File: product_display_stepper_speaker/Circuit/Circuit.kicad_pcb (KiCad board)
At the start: 2 copper layers, 1 part, among them U1 Pico

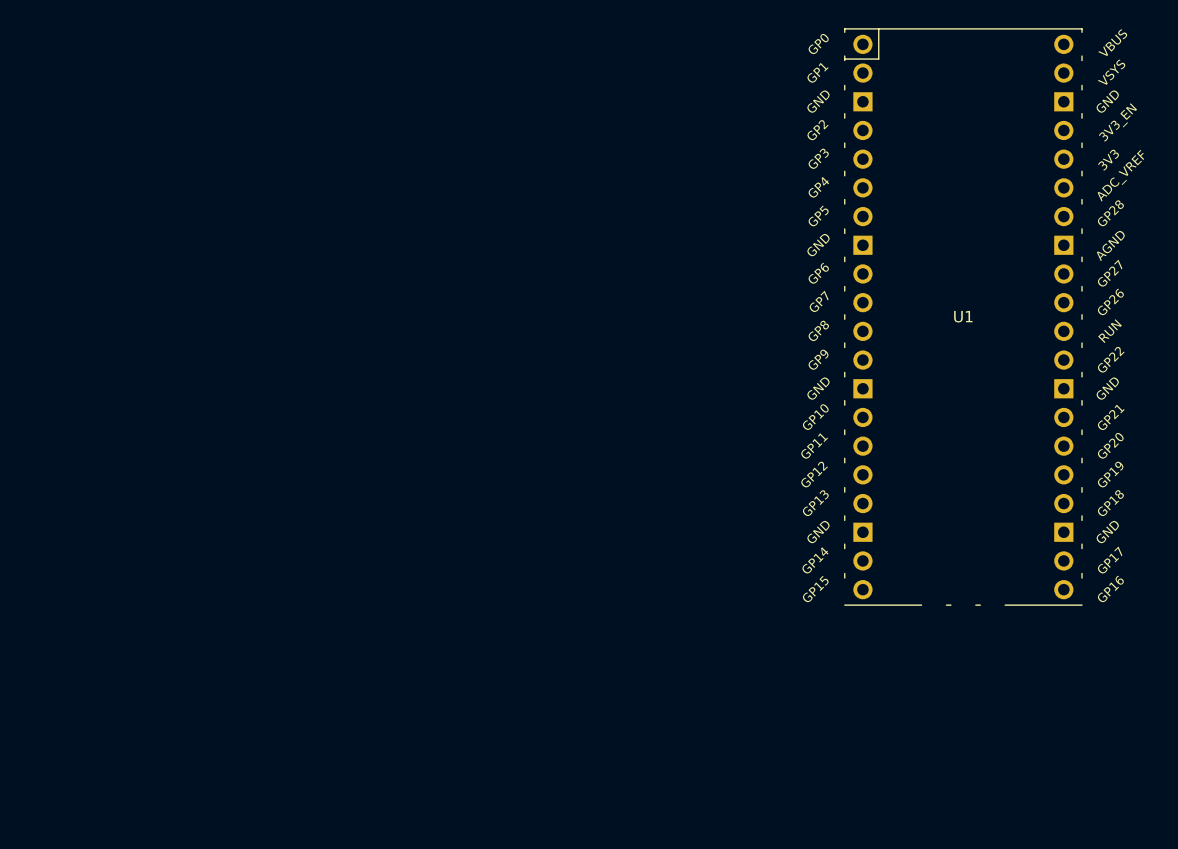
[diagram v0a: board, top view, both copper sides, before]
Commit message: finished circuit schematic and started pcb layout of product speaker stepper project
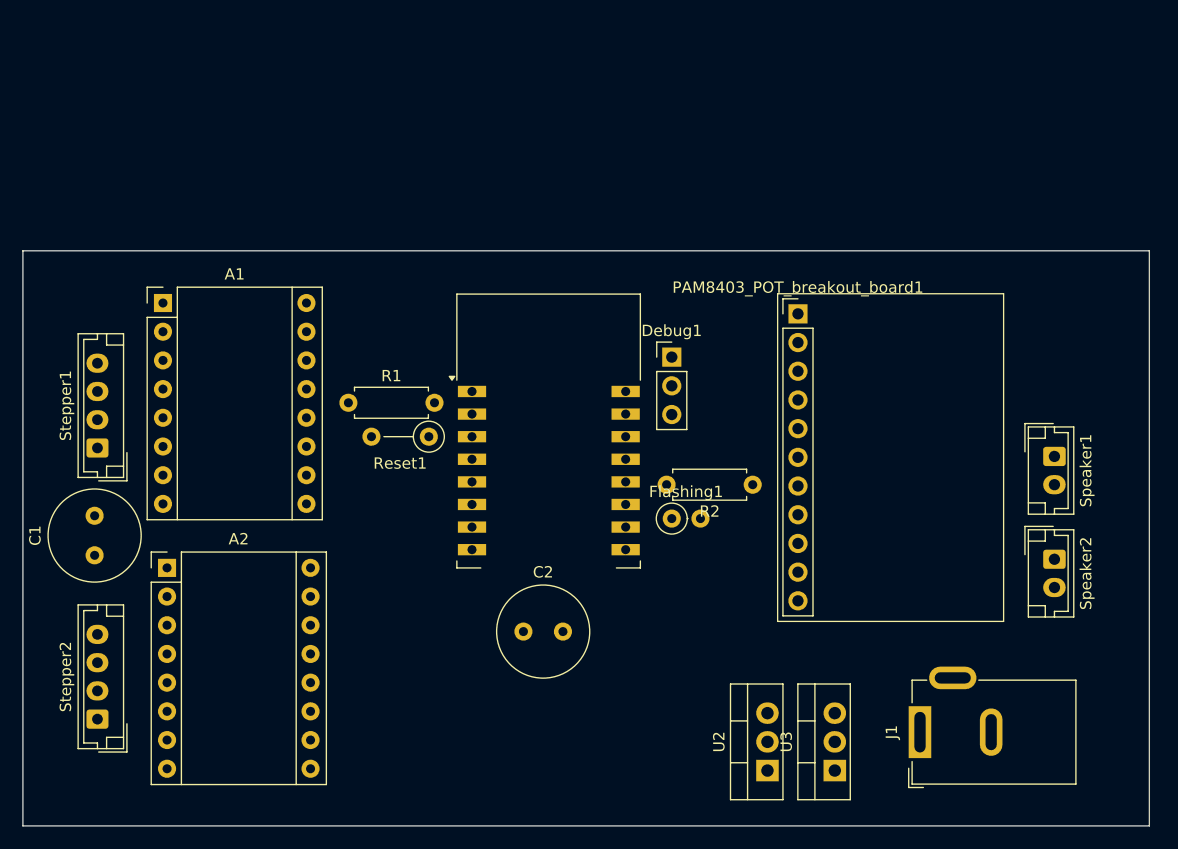
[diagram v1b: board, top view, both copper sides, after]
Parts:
- added A1: Pololu_Breakout_DRV8825, Module:Pololu_Breakout-16_15.2x20.3mm, F.Cu at (71.8, 94.4)
- added A2: Pololu_Breakout_DRV8825, Module:Pololu_Breakout-16_15.2x20.3mm, F.Cu at (72.2, 117.9)
- added C1: 470uf, Capacitor_THT:C_Radial_D8.0mm_H11.5mm_P3.50mm, F.Cu at (65.8, 116.8)
- added C2: 330uf, Capacitor_THT:C_Radial_D8.0mm_H11.5mm_P3.50mm, F.Cu at (103.7, 123.5)
- added Debug1: Conn_1x3, Connector_PinHeader_2.54mm:PinHeader_1x03_P2.54mm_Vertical, F.Cu at (116.8, 99.2)
- added Flashing1: Headers, Resistor_THT:R_Axial_DIN0207_L6.3mm_D2.5mm_P2.54mm_Vertical, F.Cu at (116.8, 113.5)
- added J1: Barrel_Jack_MountingPin, Connector_BarrelJack:BarrelJack_GCT_DCJ200-10-A_Horizontal, F.Cu at (138.8, 132.4)
- added PAM8403_POT_breakout_board1: Conn_01x11, Connector_PinHeader_2.54mm:PinHeader_1x11_P2.54mm_Vertical, F.Cu at (128.0, 95.4)
- added R1: 10k, Resistor_THT:R_Axial_DIN0207_L6.3mm_D2.5mm_P7.62mm_Horizontal, F.Cu at (88.2, 103.2)
- added R2: 10k, Resistor_THT:R_Axial_DIN0207_L6.3mm_D2.5mm_P7.62mm_Horizontal, F.Cu at (124.0, 110.5)
- added Reset1: Button, Resistor_THT:R_Axial_DIN0207_L6.3mm_D2.5mm_P5.08mm_Vertical, F.Cu at (95.3, 106.2)
- added Speaker1: JST-2p, Connector_JST:JST_EH_B2B-EH-A_1x02_P2.50mm_Vertical, F.Cu at (150.7, 108.0)
- added Speaker2: JST-2p, Connector_JST:JST_EH_B2B-EH-A_1x02_P2.50mm_Vertical, F.Cu at (150.7, 117.1)
- added Stepper1: JST-4p, Connector_JST:JST_EH_B4B-EH-A_1x04_P2.50mm_Vertical, F.Cu at (66.0, 107.2)
- added Stepper2: JST-4p, Connector_JST:JST_EH_B4B-EH-A_1x04_P2.50mm_Vertical, F.Cu at (66.0, 131.2)
- added U2: LM2931-3.3_TO220, Package_TO_SOT_THT:TO-220-3_Vertical, F.Cu at (125.3, 135.8)
- added U3: L7805, Package_TO_SOT_THT:TO-220-3_Vertical, F.Cu at (131.3, 135.8)
- U1: value Pico -> ESP-12E; footprint MCU_RaspberryPi_and_Boards:RPi_Pico_SMD_TH -> ESP:ESP-12E-DIP
- moved U1 38.2 mm to (106.0, 106.5)
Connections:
- U1 pad 15: unconnected-(U1-GPIO11-Pad15) -> GND
- U1 pad 16: unconnected-(U1-GPIO12-Pad16) -> EN
- U1 pad 17: unconnected-(U1-GPIO13-Pad17) -> GND
- U1 pad 18: unconnected-(U1-GND-Pad18) -> mode
- U1 pad 19: unconnected-(U1-GPIO14-Pad19) -> speaker_r
- U1 pad 20: unconnected-(U1-GPIO15-Pad20) -> speaker_r
- U1 pad 21: unconnected-(U1-GPIO16-Pad21) -> /RX
- U1 pad 22: unconnected-(U1-GPIO17-Pad22) -> /TX
- U1 pad 3: unconnected-(U1-GND-Pad3) -> Reset
- U1 pad 4: unconnected-(U1-GPIO2-Pad4) -> DIR2
- U1 pad 5: unconnected-(U1-GPIO3-Pad5) -> STEP2
- U1 pad 6: unconnected-(U1-GPIO4-Pad6) -> STEP1
- U1 pad 7: unconnected-(U1-GPIO5-Pad7) -> DIR1
- U1 pad 8: unconnected-(U1-GND-Pad8) -> +3.3V
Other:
- board outline added: 99.7 x 50.9 mm

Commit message: almost finished pcb layout solution
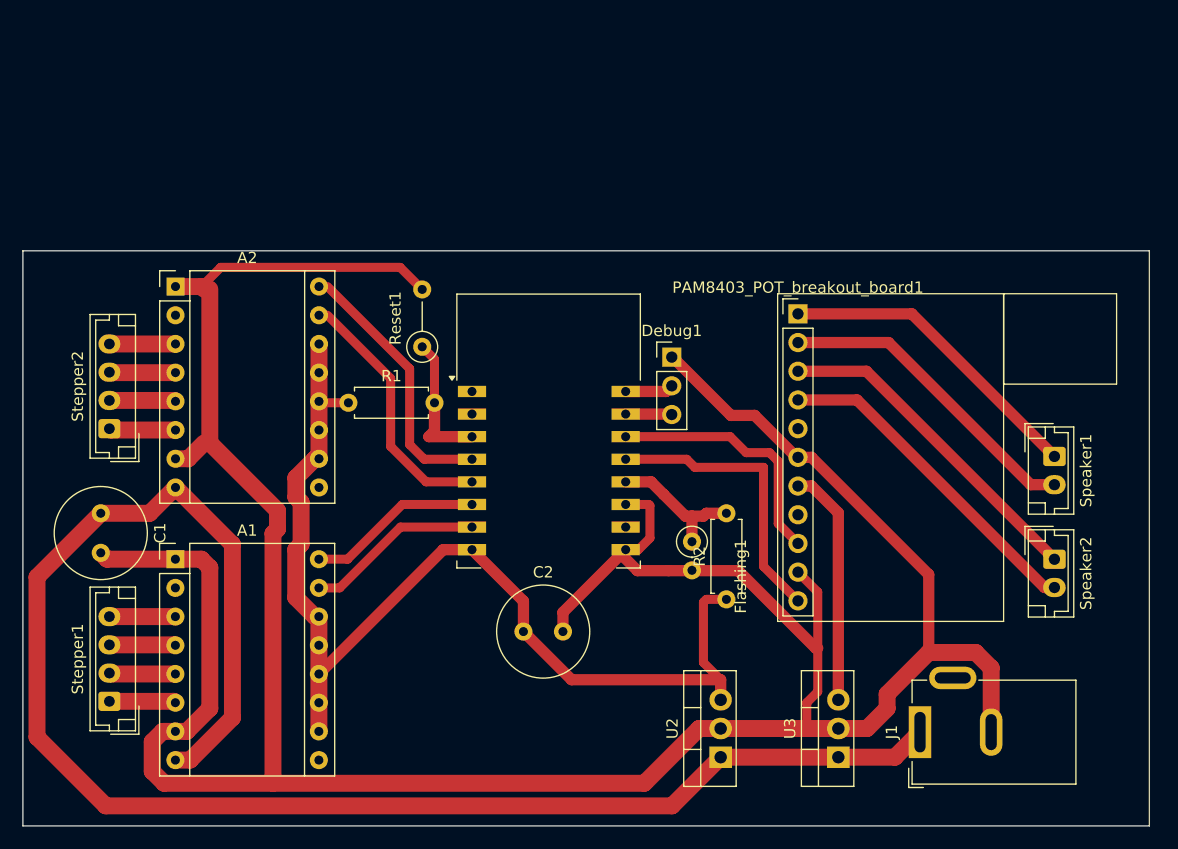
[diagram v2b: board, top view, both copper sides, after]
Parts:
- moved Stepper2 25.7 mm to (67.1, 105.5)
- moved A2 24.9 mm to (72.9, 93.0)
- moved A1 22.7 mm to (72.9, 117.1)
- moved Stepper1 22.4 mm to (67.1, 129.7)
- moved R2 10.4 mm to (121.7, 120.7), turned to 90 degrees
- moved Reset1 7.97 mm to (94.7, 98.3), turned to 90 degrees
- moved U2 4.31 mm to (121.2, 134.6)
- moved C1 3.76 mm to (66.3, 113.0), turned to -90 degrees
- moved Flashing1 2.71 mm to (118.6, 115.5), turned to -90 degrees
- moved U3 1.22 mm to (131.6, 134.6)
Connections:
- U1 pad 19: speaker_r -> speaker_l
- U1 pad 6: STEP1 -> DIR1
- U1 pad 7: DIR1 -> STEP1
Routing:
- net GND: track 0.00 -> 281.8 mm
- net +12V: track 0.00 -> 142.2 mm
- net +3.3V: track 0.00 -> 97.3 mm
- net Net-(PAM8403_POT_breakout_board1-Pin_3): track 0.00 -> 29.6 mm
- net Net-(PAM8403_POT_breakout_board1-Pin_4): track 0.00 -> 29.6 mm
- net Net-(PAM8403_POT_breakout_board1-Pin_1): track 0.00 -> 27.9 mm
- net Net-(PAM8403_POT_breakout_board1-Pin_2): track 0.00 -> 27.9 mm
- net speaker_l: track 0.00 -> 25.6 mm
- net DIR2: track 0.00 -> 23.1 mm
- net speaker_r: track 0.00 -> 22.5 mm
- net STEP2: track 0.00 -> 22.4 mm
- net +5V: track 0.00 -> 21.1 mm
- net STEP1: track 0.00 -> 15.8 mm
- net DIR1: track 0.00 -> 15.6 mm
- net mode: track 0.00 -> 12.5 mm
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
